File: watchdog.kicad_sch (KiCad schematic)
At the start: 0 parts

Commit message: Started working on watchdog circuit.
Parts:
- added C20: 1uF, symbol Device:C
- added C21: 0.22uF, symbol Device:C
- added C22: 4.7uF, symbol Device:C
- added D4: 1N4148W-7-F, Diode_SMD:D_SOD-123, symbol Device:D
- added R29, R30, R31: 470K, symbol Device:R_US
- added R32: 100K, Resistor_SMD:R_0402_1005Metric, symbol #inventree_kicad:R_100K_0402_1PCT_0W0625
- added R33, R34, R35: 33R, symbol Device:R_US
- added U6: 74HC4060, symbol 74xx:74HC4060
- added U7: 74HC14BQ,115, symbol 74xx:74HC14
- added U8: 74HC02, symbol 74xx:74HC02
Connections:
- new net AUDIO_DETECT: U7.2, U8.9
- new net AUDIO_IN: C20.2
- new net C_AUDIO_IN: C20.1, D4.2 (A), R29.2
- new net ENV_HOLD: C21.1, D4.1 (K), R30.2
- new net ENV_THRESHOLD: R30.1, R31.1, U7.1
- new net GND: C21.2, C22.1, R29.1, R31.2
- new net POR_IN: C22.2, R32.2, U7.3
- new net POR_OUT: R33.1, U8.8
- new net S_POR_OUT: R33.2, U7.4
- new net S_WAKE: R35.2, U8.13
- new net V_{SYS}: R32.1
- new net WAKE: R35.1, U6.12 (CLR)
- new net ~{S_WAKE}: R34.2, U8.10
- new net ~{WAKE}: R34.1, U8.11, U8.12
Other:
- note added: "74HC14BQ,115"
- note added: "Envelope Detector"
- note added: "Power-on reset"
- note added: "Threshold Adj Lab: Tune"
- note added: "V_{C} = V_{S} * (1 - e^{-t/(RC)}) Min time at 3V: 120ms Min time at 4.2V: 85ms Mine time at 5V: 70ms"

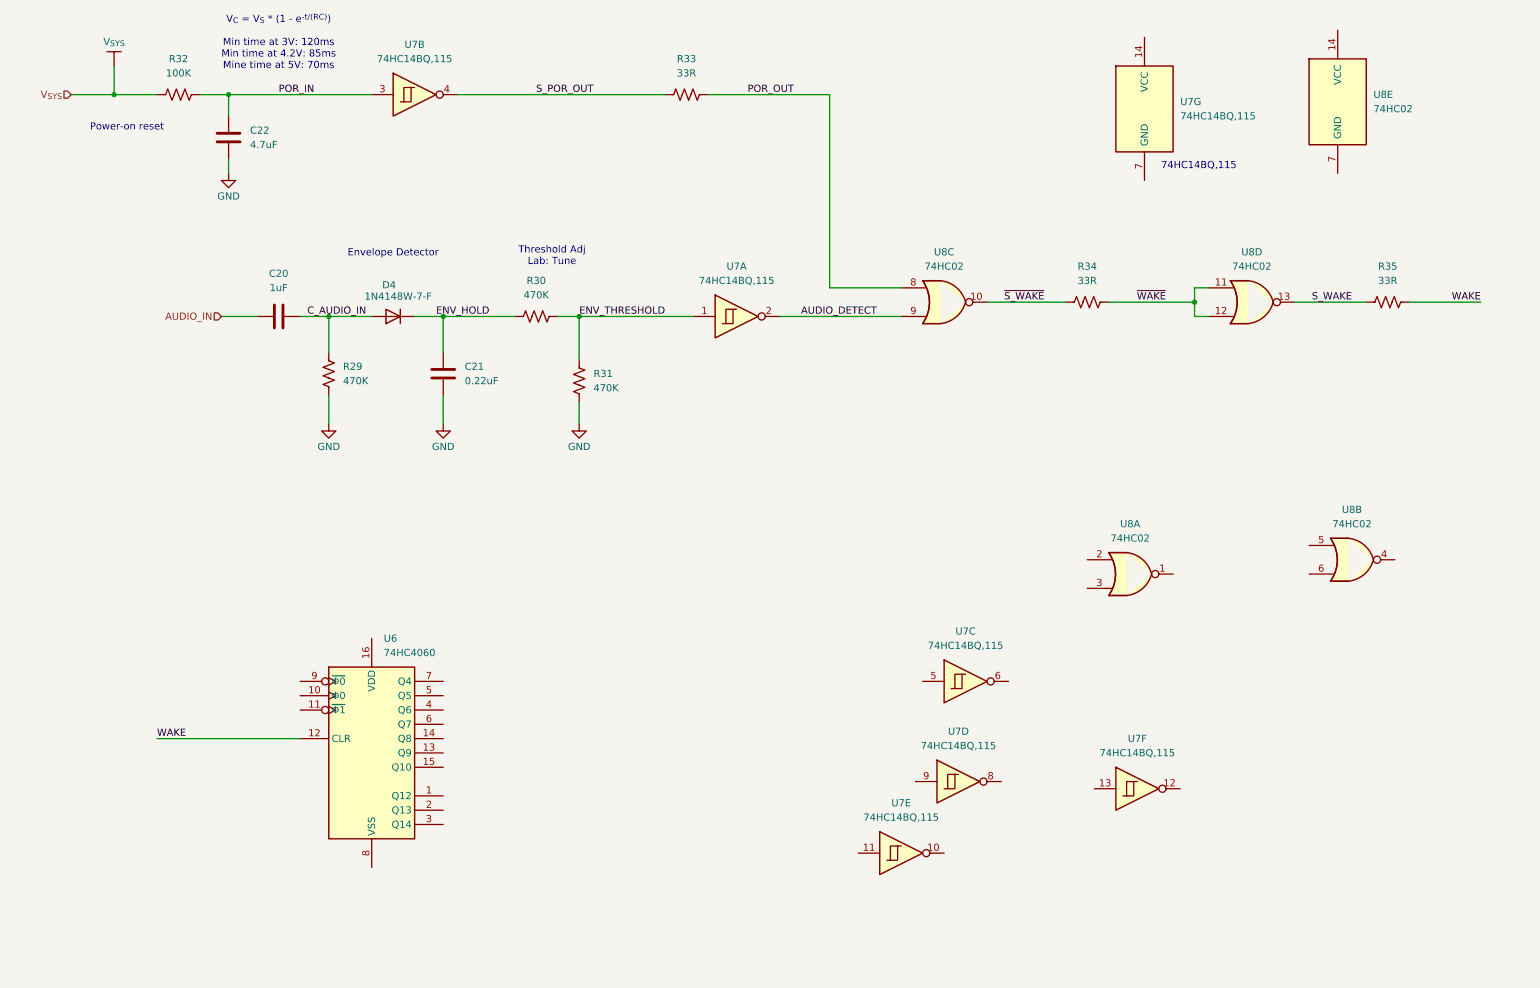
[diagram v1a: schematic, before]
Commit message: Finalizing watchdog and boost circuit.
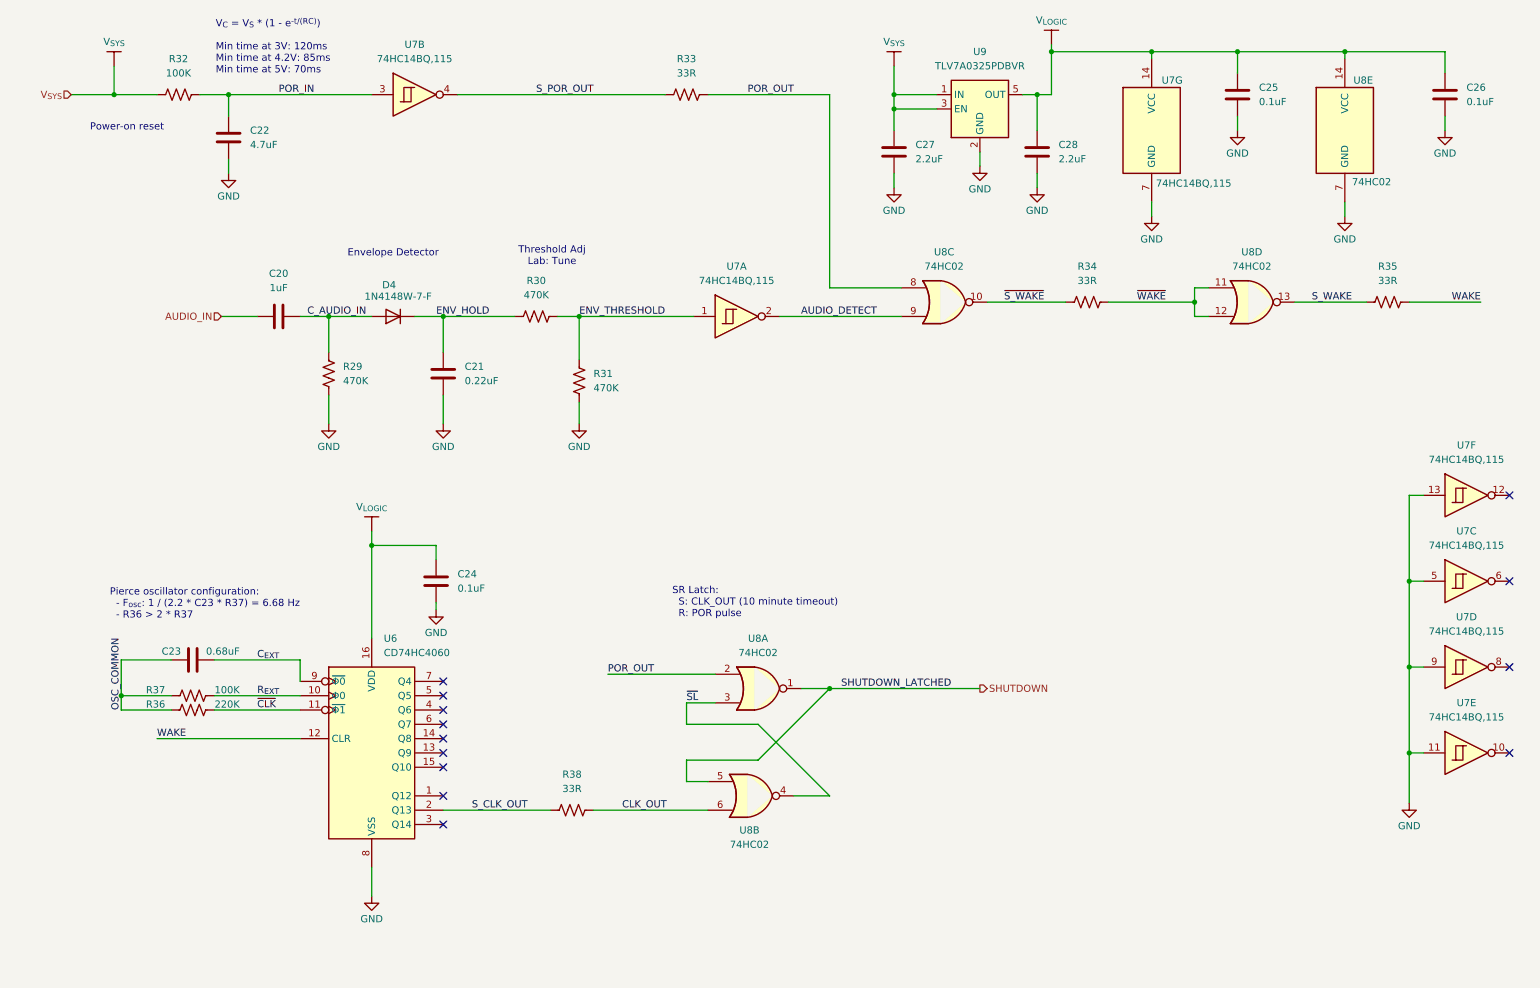
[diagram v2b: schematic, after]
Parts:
- added C23: 0.68uF, symbol Device:C
- added C24, C25, C26: 0.1uF, Capacitor_SMD:C_0402_1005Metric, symbol #inventree_kicad:C_0U1_X7R_16V_0402
- added C27, C28: 2.2uF, symbol Device:C
- added R36: 220K, symbol Device:R_US
- added R37: 100K, symbol Device:R_US
- added R38: 33R, symbol Device:R_US
- added U9: TLV7A0325PDBVR, Package_TO_SOT_SMD:SOT-23-5, symbol Regulator_Linear:TPS7A0508PDBV
- U6: value 74HC4060 -> CD74HC4060
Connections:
- net GND: now also U6.8 (VSS), U7.11, U7.13, U7.5, U7.7 (GND), U7.9, U8.7 (GND), C24.2, C25.2, C26.2, C27.1, C28.1, U9.2 (GND)
- net POR_OUT: now also U8.2
- net V_{SYS}: now also C27.2, U9.1 (IN), U9.3 (EN)
- net ~{SL}: now reaches U8.4
- net ~{SL}: now also U8.3
- net SHUTDOWN: now reaches U8.5
- net SHUTDOWN: now also U8.1
- net CLK_OUT: now reaches U8.6
- net CLK_OUT: now also R38.1
- net V_{LOGIC}: now reaches U7.14 (VCC)
- net V_{LOGIC}: now also U6.16 (VDD), U8.14 (VCC), C24.1, C25.1, C26.1, C28.2, U9.5 (OUT)
- net R_{EXT}: now reaches U6.10 (Φ0)
- net R_{EXT}: now also R37.1
- net ~{CLK}: now reaches U6.11 (~{Φ1})
- net ~{CLK}: now also R36.1
- net S_CLK_OUT: now reaches U6.2 (Q13)
- net S_CLK_OUT: now also R38.2
- net C_{EXT}: now reaches U6.9 (~{Φ0})
- net C_{EXT}: now also C23.1
- new net OSC_COMMON: C23.2, R36.2, R37.2
- no-connect marks 0 -> 13
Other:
- note added: "Pierce oscillator configuration: - F_{osc}: 1 / (2.2 * C23 * R37) = 6.68 Hz - R36 > 2 * R37"
- note added: "SR Latch: S: CLK_OUT (10 minute timeout) R: POR pulse"
- note added: "V_{C} = V_{S} * (1 - e^{-t/(RC)}) Min time at 3V: 120ms Min time at 4.2V: 85ms Min time at 5V: 70ms"
- note removed: "74HC14BQ,115"
- note removed: "V_{C} = V_{S} * (1 - e^{-t/(RC)}) Min time at 3V: 120ms Min time at 4.2V: 85ms Mine time at 5V: 70ms"
- moved on the sheet: U7C, U7D, U7E, U7F, U7G, U8A, U8B, U8E

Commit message: First rough draft of schematics complete -- missing a lot of PLM/Inventree work. Ran through several Claude reviews.
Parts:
- added R47: 33R, symbol Device:R_US
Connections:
- net SHUTDOWN: now also R47.1; no longer U8.1, U8.5
- new net SHUTDOWN_LATCHED: R47.2, U8.1, U8.5
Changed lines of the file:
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@@
 	(wire
 		(pts
-			(xy 154.94 134.62) (xy 181.61 134.62)
+			(xy 154.94 134.62) (xy 185.42 134.62)
 		)
 		(stroke
@@
 		(pts
 			(xy 166.37 29.21) (xy 166.37 31.75)
+		)
+		(stroke
+			(width 0)
+			(type default)
+		)
+	)
+	(wire
+		(pts
+			(xy 193.04 134.62) (xy 204.47 134.62)
 		)
 		(stroke
@@
 	)
 	(label "SHUTDOWN_LATCHED"
-		(at 176.53 134.62 180)
+		(at 179.07 134.62 180)
 		(effects
 			(font
@@
 	(hierarchical_label "SHUTDOWN"
 		(shape output)
-		(at 181.61 134.62 0)
+		(at 204.47 134.62 0)
 		(effects
 			(font
@@
 				)
 			)
+		)
+	)
+	(symbol
+		(lib_id "Device:R_US")
+		(at 189.23 134.62 270)
+		(unit 1)
+		(body_style 1)
+		(exclude_from_sim no)
+		(in_bom yes)
+		(on_board yes)
+		(in_pos_files yes)
+		(dnp no)
+		(fields_autoplaced yes)
+		(property "Reference" "R47"
+			(at 189.23 128.27 90)
+			(show_name no)
+			(do_not_autoplace no)
+			(effects
+				(font
+					(size 1.27 1.27)
+				)
+			)
+		)
+		(property "Value" "33R"
+			(at 189.23 130.81 90)
+			(show_name no)
+			(do_not_autoplace no)
+			(effects
+				(font
+					(size 1.27 1.27)
+				)
+			)
+		)
+		(property "Footprint" ""
+			(at 188.976 135.636 90)
+			(hide yes)
+			(show_name no)
+			(do_not_autoplace no)
+			(effects
+				(font
+					(size 1.27 1.27)
+				)
+			)
+		)
+		(property "Datasheet" ""
+			(at 189.23 134.62 0)
+			(hide yes)
+			(show_name no)
+			(do_not_autoplace no)
+			(effects
+				(font
+					(size 1.27 1.27)
+				)
+			)
+		)
+		(property "Description" "Resistor, US symbol"
+			(at 189.23 134.62 0)
+			(hide yes)
+			(show_name no)
+			(do_not_autoplace no)
+			(effects
+				(font
+					(size 1.27 1.27)
+				)
+			)
+		)
+		(pin "2"
+		)
+		(pin "1"
+		)
+		(instances
+			(project "headphone_amp"
+				(path "/62ffec33-ae93-49a8-bfe6-566578dd8e82/9e81eff7-fa8a-4d9c-b865-cbf1c6348e7c"
+					(reference "R47")
+					(unit 1)
+				)
+			)

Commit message: Started Inventree work.
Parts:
- R33, R34, R35, R38, R47: footprint (none) -> Resistor_SMD:R_0402_1005Metric; symbol Device:R_US -> #inventree_kicad:R_33R_0402_1PCT_0W0625; IPN (none) -> 302-0011; InvenTree (none) -> 28; Part URL (none) -> http://10.0.0.33/web/part/28/
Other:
- note added: "Q13 - 10.2 minutes"
- moved on the sheet: C23, C24, R36, R37, R38, R47, U6, U7C, U7D, U7E, U7F, U8A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

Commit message: Started adding new parts to inventree and re-synchronizing here.
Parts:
- R29, R30, R31: footprint (none) -> Resistor_SMD:R_0402_1005Metric; symbol Device:R_US -> #inventree_kicad:R_470K_0402_1PCT_0W0625; IPN (none) -> 302-0014; InvenTree (none) -> 34; Part URL (none) -> http://10.0.0.33/web/part/34/
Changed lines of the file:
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@@
 	)
 	(symbol
-		(lib_id "Device:R_US")
+		(lib_id "#inventree_kicad:R_470K_0402_1PCT_0W0625")
 		(at 102.87 68.58 270)
 		(unit 1)
@@
 			)
 		)
-		(property "Footprint" ""
+		(property "Footprint" "Resistor_SMD:R_0402_1005Metric"
 			(at 102.616 69.596 90)
 			(hide yes)
@@
 			)
 		)
-		(property "Description" "Resistor, US symbol"
+		(property "Description" "470 kOhm ±1% 0.063W, 1/16W Chip Resistor 0402 (1005 Metric)"
+			(at 102.87 68.58 0)
+			(hide yes)
+			(show_name no)
+			(do_not_autoplace no)
+			(effects
+				(font
+					(size 1.27 1.27)
+				)
+			)
+		)
+		(property "IPN" "302-0014"
+			(at 102.87 68.58 0)
+			(hide yes)
+			(show_name no)
+			(do_not_autoplace no)
+			(effects
+				(font
+					(size 1.27 1.27)
+				)
+			)
+		)
+		(property "InvenTree" "34"
+			(at 102.87 68.58 0)
+			(hide yes)
+			(show_name no)
+			(do_not_autoplace no)
+			(effects
+				(font
+					(size 1.27 1.27)
+				)
+			)
+		)
+		(property "Part URL" "http://10.0.0.33/web/part/34/"
 			(at 102.87 68.58 0)
 			(hide yes)
@@
 	)
 	(symbol
-		(lib_id "Device:R_US")
+		(lib_id "#inventree_kicad:R_470K_0402_1PCT_0W0625")
 		(at 110.49 80.01 0)
 		(unit 1)
@@
 			)
 		)
-		(property "Footprint" ""
+		(property "Footprint" "Resistor_SMD:R_0402_1005Metric"
 			(at 111.506 80.264 90)
 			(hide yes)
@@
 			)
 		)
-		(property "Description" "Resistor, US symbol"
+		(property "Description" "470 kOhm ±1% 0.063W, 1/16W Chip Resistor 0402 (1005 Metric)"
+			(at 110.49 80.01 0)
+			(hide yes)
+			(show_name no)
+			(do_not_autoplace no)
+			(effects
+				(font
+					(size 1.27 1.27)
+				)
+			)
+		)
+		(property "IPN" "302-0014"
+			(at 110.49 80.01 0)
+			(hide yes)
+			(show_name no)
+			(do_not_autoplace no)
+			(effects
+				(font
+					(size 1.27 1.27)
+				)
+			)
+		)
+		(property "InvenTree" "34"
+			(at 110.49 80.01 0)
+			(hide yes)
+			(show_name no)
+			(do_not_autoplace no)
+			(effects
+				(font
+					(size 1.27 1.27)
+				)
+			)
+		)
+		(property "Part URL" "http://10.0.0.33/web/part/34/"
 			(at 110.49 80.01 0)
 			(hide yes)
@@
 	)
 	(symbol
-		(lib_id "Device:R_US")
+		(lib_id "#inventree_kicad:R_470K_0402_1PCT_0W0625")
 		(at 66.04 78.74 180)
 		(unit 1)
@@
 			)
 		)
-		(property "Footprint" ""
+		(property "Footprint" "Resistor_SMD:R_0402_1005Metric"
 			(at 65.024 78.486 90)
 			(hide yes)
@@
 			)
 		)
-		(property "Description" "Resistor, US symbol"
+		(property "Description" "470 kOhm ±1% 0.063W, 1/16W Chip Resistor 0402 (1005 Metric)"
 			(at 66.04 78.74 0)
 			(hide yes)
+			(show_name no)
+			(do_not_autoplace no)
+			(effects
+				(font
+					(size 1.27 1.27)
+				)
+			)
+		)
+		(property "IPN" "302-0014"
+			(at 66.04 78.74 0)
+			(hide yes)
+			(show_name no)
+			(do_not_autoplace no)
+			(effects
+				(font
+					(size 1.27 1.27)
+				)
+			)
+		)
+		(property "InvenTree" "34"
+			(at 66.04 78.74 0)
+			(hide yes)
+			(show_name no)
+			(do_not_autoplace no)
+			(effects
+				(font
+					(size 1.27 1.27)
+				)
+			)
+		)
+		(property "Part URL" "http://10.0.0.33/web/part/34/"
+			(at 66.04 78.74 0)
+			(hide yes)

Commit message: Preliminary layout complete, done on airpane so needs verification.
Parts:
- C20, C22, C27, C28: footprint (none) -> Capacitor_SMD:C_0603_1608Metric
- C21, C23: footprint (none) -> Capacitor_SMD:C_0402_1005Metric
- R37: footprint (none) -> Resistor_SMD:R_0402_1005Metric
- U6: footprint (none) -> Package_SO:TSSOP-16_4.4x5mm_P0.65mm
- U7: footprint (none) -> Package_DFN_QFN:DHVQFN-14-1EP_2.5x3mm_P0.5mm_EP1x1.5mm
- U8: footprint (none) -> Package_SO:TSSOP-14_4.4x5mm_P0.65mm
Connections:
- net GND: now also U7.15 (EPAD)

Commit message: Started adding some 3D models and footprints.
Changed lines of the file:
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@@
 		(in_pos_files yes)
 		(dnp no)
-		(fields_autoplaced yes)
 		(property "Reference" "U7"
-			(at 140.208 59.69 0)
+			(at 134.62 62.992 0)
 			(show_name no)
 			(do_not_autoplace no)
@@
 		)
 		(property "Value" "74HC14BQ,115"
-			(at 140.97 77.978 0)
+			(at 131.318 74.93 0)
 			(show_name no)
 			(do_not_autoplace no)
@@
 		(in_pos_files yes)
 		(dnp no)
-		(fields_autoplaced yes)
 		(property "Reference" "U7"
-			(at 83.058 20.32 0)
+			(at 77.724 22.86 0)
 			(show_name no)
 			(do_not_autoplace no)
@@
 		)
 		(property "Value" "74HC14BQ,115"
-			(at 83.82 38.608 0)
+			(at 75.184 35.814 0)
 			(show_name no)
 			(do_not_autoplace no)
